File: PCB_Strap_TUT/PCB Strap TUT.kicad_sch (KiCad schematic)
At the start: 45 parts, among them J1 Debug, Q1 Q_PMOS_GDS, SW1 SW_SPST, U1 PIC16F1503-ISL

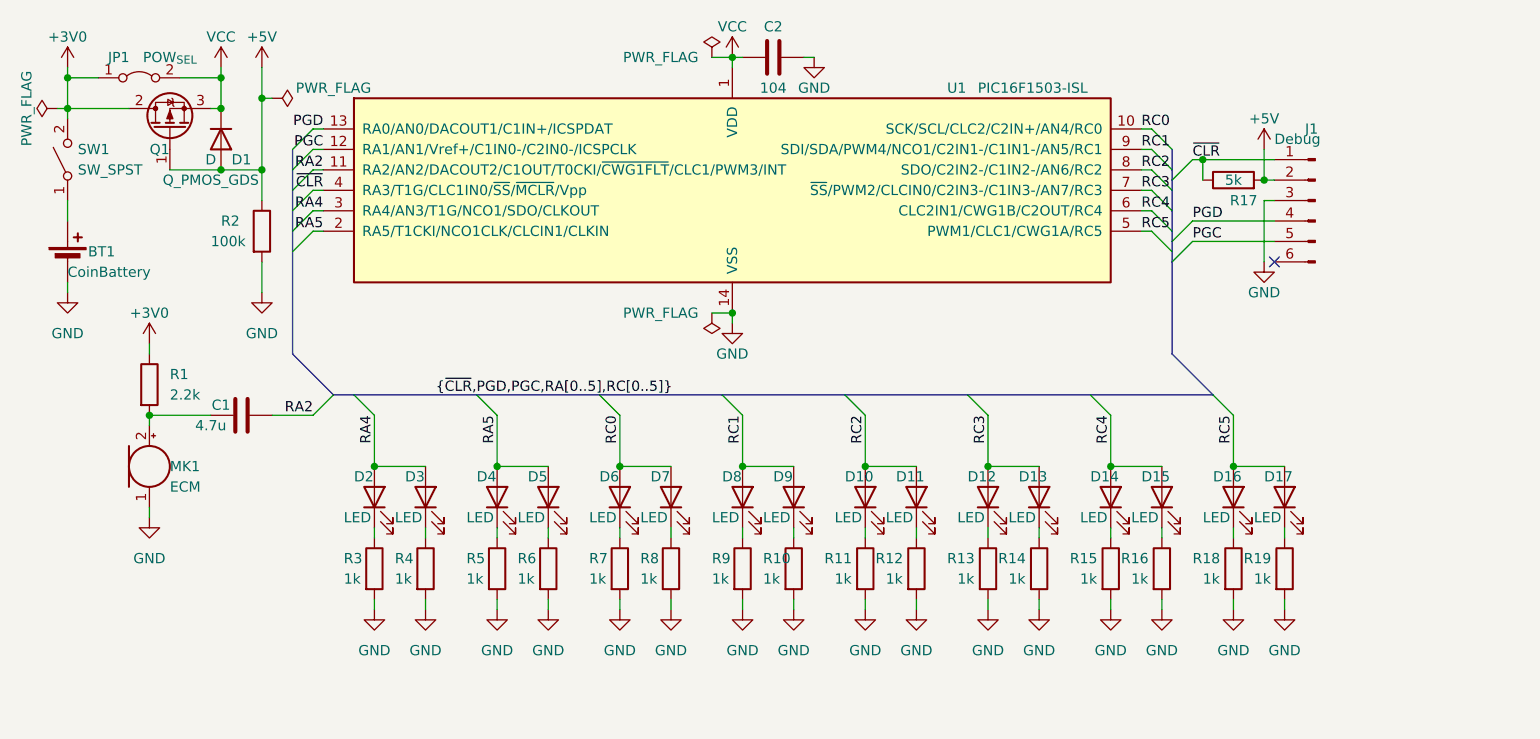
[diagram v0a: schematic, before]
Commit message: test ADC and add Amp
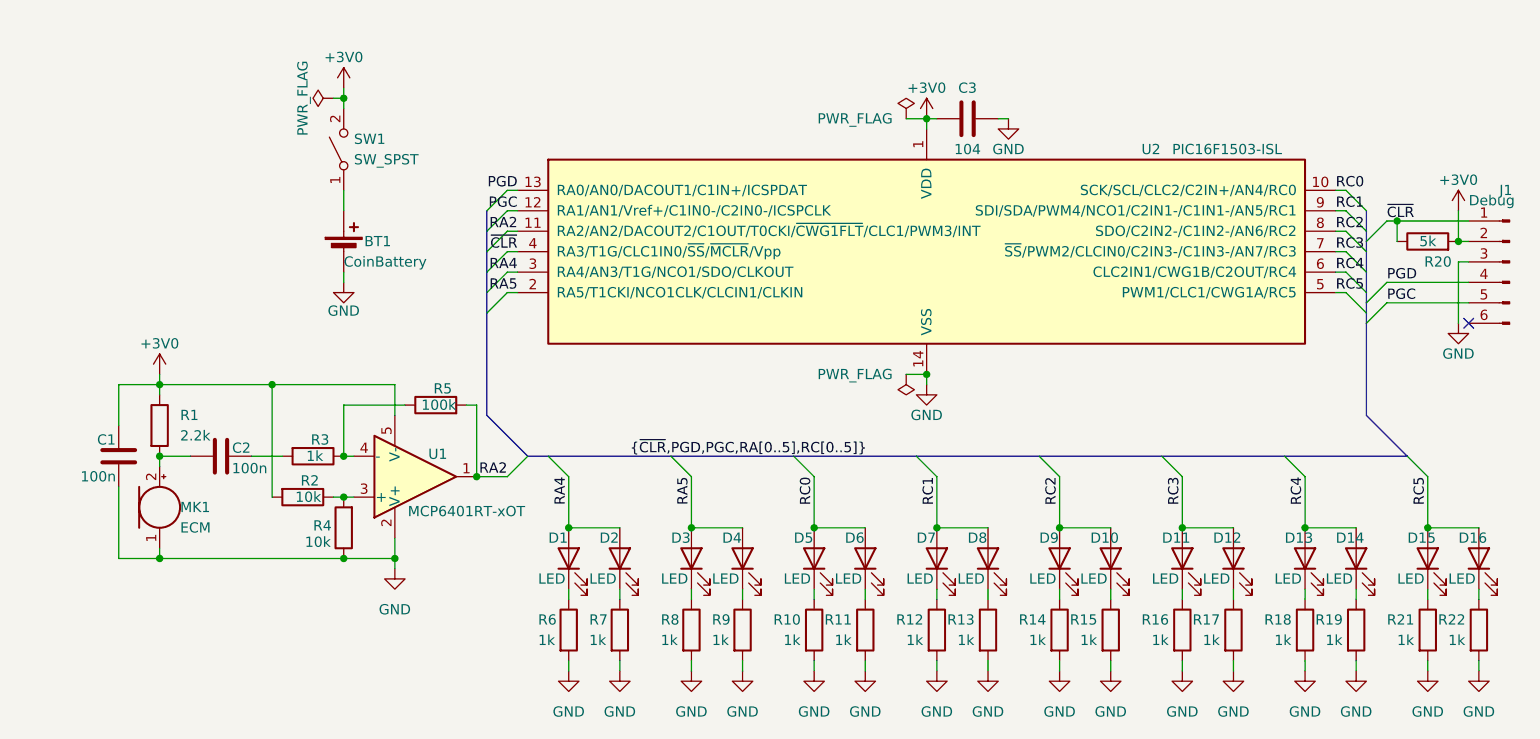
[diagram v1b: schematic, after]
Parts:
- removed D1: D, Diode_THT:D_A-405_P7.62mm_Horizontal, symbol Device:D
- removed JP1: POW_{SEL}, Jumper:SolderJumper-2_P1.3mm_Bridged_Pad1.0x1.5mm, symbol Jumper:Jumper_2_Bridged
- removed Q1: Q_PMOS_GDS, Package_TO_SOT_THT:TO-251-3_Vertical, symbol Device:Q_PMOS_GDS
- added C1: 100n, Capacitor_SMD:C_0402_1005Metric, symbol Device:C
- added R3: 1k, Resistor_SMD:R_0603_1608Metric, symbol Device:R
- added R4: 10k, Resistor_SMD:R_0603_1608Metric, symbol Device:R
- added R5: 100k, Resistor_SMD:R_0603_1608Metric, symbol Device:R
- added U1: MCP6401RT-xOT, Package_TO_SOT_SMD:SOT-23-5, symbol Amplifier_Operational:MCP6401RT-xOT
- C2: renamed from C1; value 4.7u -> 100n
- R2: value 100k -> 10k
- renumbered C2 to C3, D2 to D1, D11 to D10, D12 to D11, D13 to D12, D14 to D13, D15 to D14, D16 to D15, D17 to D16, D3 to D2, D4 to D3, D5 to D4, D6 to D5, D7 to D6, D8 to D7, D9 to D8, D10 to D9, R7 to R10, R8 to R11, R9 to R12, R10 to R13, R11 to R14, R12 to R15, R13 to R16, R14 to R17, R15 to R18, R16 to R19, R17 to R20, R18 to R21, R19 to R22, R3 to R6, R4 to R7, R5 to R8, R6 to R9, U1 to U2
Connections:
- net VCC is gone; now on net +3V0: C3.1, U2.1 (VDD)
- net +3V0: now also J1.2 (Pin_2), R2.2, R20.2, C1.2, U1.5 (V-)
- net GND: now also C1.1, R4.1, U1.2 (V+); no longer R2.2
- net RA2: now also R5.2, U1.1; no longer C2.2
- removed net +5V: J1.2 (Pin_2), R2.1, R20.2
- new net: R2.1, R4.2, U1.3 (+)
- new net: R3.1, R5.1, U1.4 (-)
- new net: C2.2, R3.2
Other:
- moved on the sheet: BT1, C2, C3, D1, D10, D11, D12, D13, D14, D15, D16, D2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
